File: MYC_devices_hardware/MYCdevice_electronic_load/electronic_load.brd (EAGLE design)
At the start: 136.5 x 53.6 mm, 129 parts, among them IC1 MEGA16-P, IC10 Gate7, IC11 LF347N, IC12 LF347N, IC14 MCP603CH, IC15 MCP603CH, IC16 MCP603CH, IC17 MCP603CH, IC18 MCP603CH, IC19 MCP603CH, IC2 MAX232, IC20 MCP603CH, IC3 7805TV, IC4 Gate1, IC5 Gate2, IC6 Gate3, IC7 Gate4, IC8 Gate5, IC9 Gate6, Q1 20MHz, X1 8-15V, X2 1503_09, X3 1503_09, X4 RS232

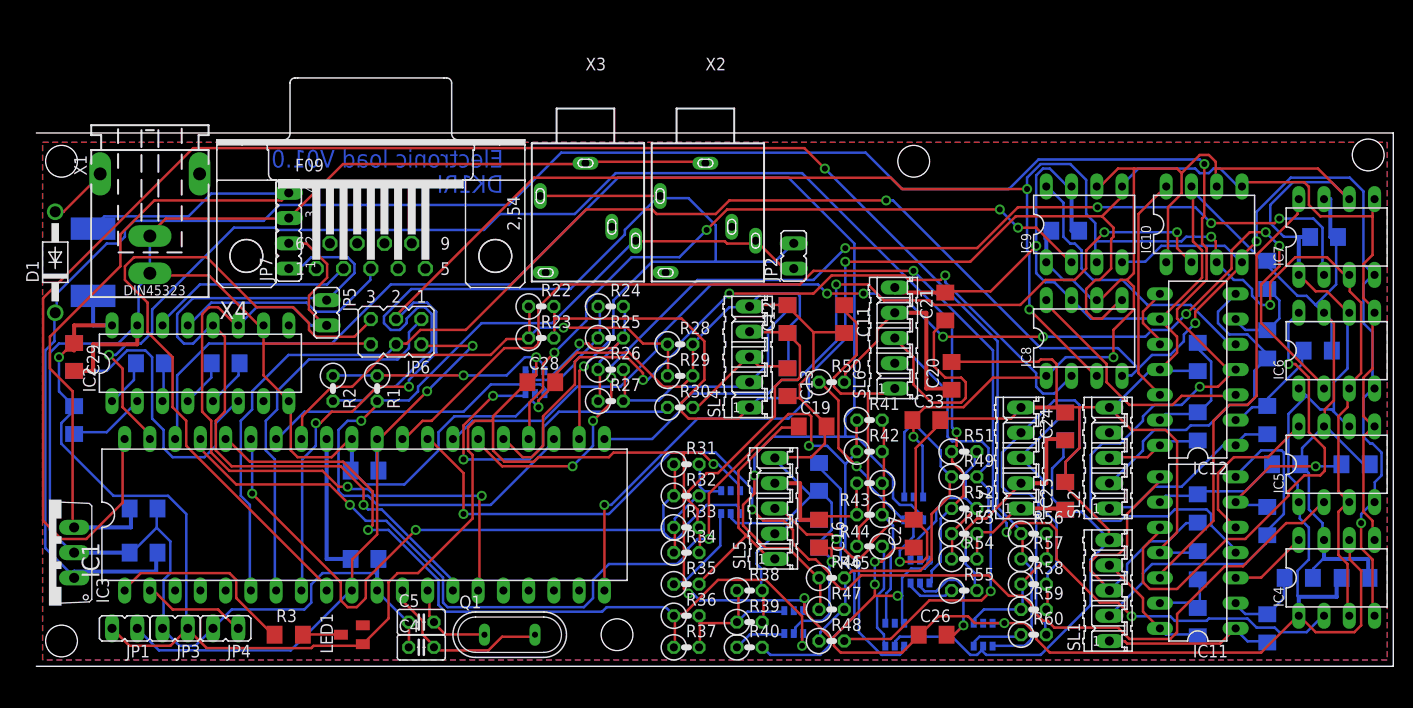
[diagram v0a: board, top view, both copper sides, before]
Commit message: deleted duplicate MYCdevice_electronic_load
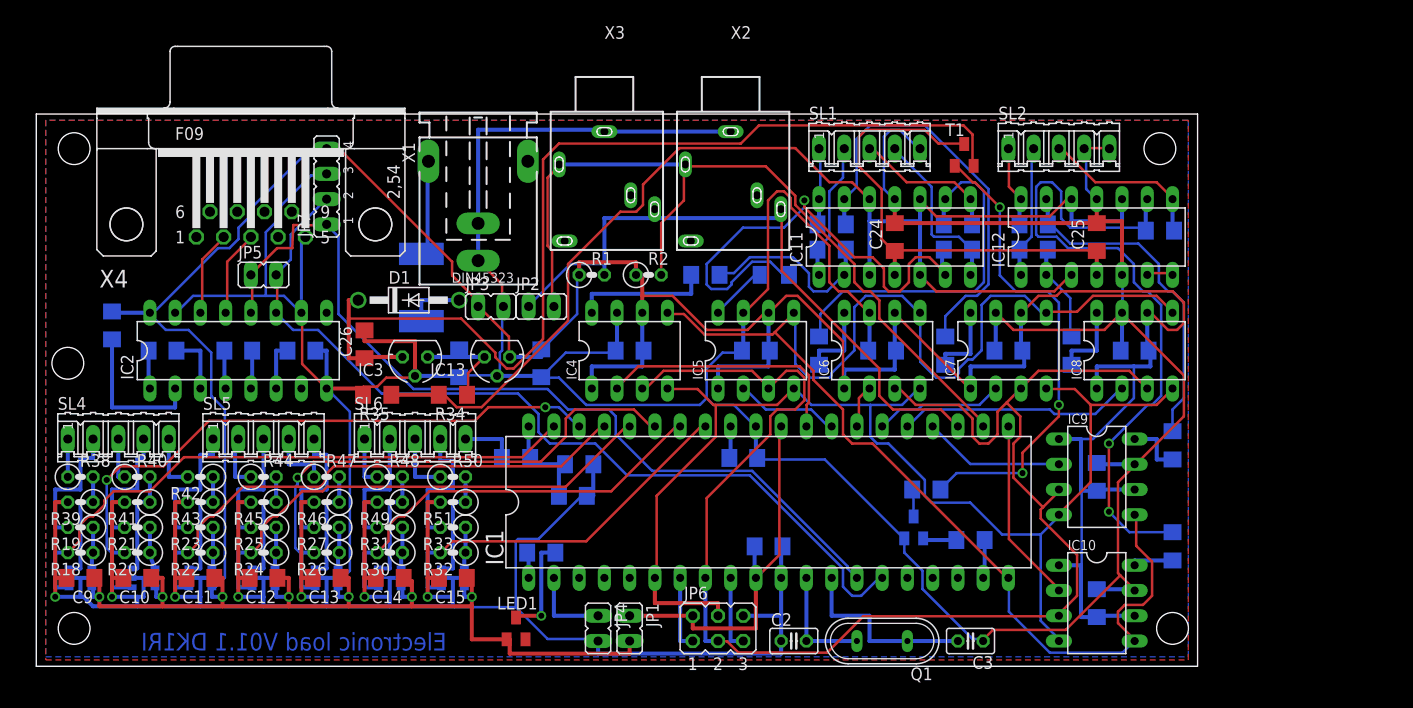
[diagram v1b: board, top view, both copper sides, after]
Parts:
- removed C29, C30, C31, C32, C33: 22uF 1210, rcl:C1206
- removed R52, R57: 27k, resistor:0207/2V
- removed R53, R58: 1k 1%, resistor:0207/2V
- removed R54: 9k53, resistor:0207/2V
- removed R55, R60: 22k, resistor:0207/2V
- removed R56: 9k1 1%, resistor:0207/2V
- removed R59: 9k52, resistor:0207/2V
- removed SL7: U/Iin, con-amp-quick:05P
- added IC13: 78L5, v-reg:78LXX
- added R18, R20: 154k, resistor:0207/2V
- added R19, R21: 18k, resistor:0207/2V
- added T1: BC807, transistor:SOT23-BEC
- added T2: BC817, transistor:SOT23-BEC
- C10, C9: value 22u 1210 -> 22uF 1210
- C11, C12, C13, C14, C15, C16, C17, C18, C19, C20, C21, C22, C23, C24, C25: value 22u -> 22uF 1210; device resistor:C1206 -> rcl:C1206
- C2, C3: value 22uF 1210 -> 18pF; device rcl:C1206 -> resistor:C025-025X050
- C28: value 22uF 1210 -> 1u; device rcl:C1206 -> resistor:C1206
- C4: value 18pF -> 22uF 1210; device resistor:C025-025X050 -> rcl:C1206
- C5: value 18pF -> 22u 1210; device resistor:C025-025X050 -> rcl:C1206
- C6: value 22uF 1210 -> 22u 1210
- IC10: value Gate7 -> MCP4921
- IC11, IC12: value LF347N -> LM324N
- IC3: value 7805TV -> 79L09; device linear:TO220V -> v-reg:78LXX
- IC4: value Gate1 -> MCP4921
- IC5: value Gate2 -> MCP4921
- IC6: value Gate3 -> MCP4921
- IC7: value Gate4 -> MCP4921
- IC8: value Gate5 -> MCP4921
- IC9: value Gate6 -> MCP4921
- L1: value (none) -> 22u
- R10, R12, R14, R16, R4, R6, R8: value 10k -> 12k
- R11, R13, R15, R17, R5, R7, R9: value 10k -> 8k2
- R22: value 68k 1% -> 154k
- R23: value na -> 18k
- R24: value 9k1 1% -> 154k
- R25: value 27k -> 18k
- R26, R38, R48: value 1k 1% -> 154k
- R27, R39, R49: value 9k53 -> 18k
- R28: value 1,8 1% -> 1k5; device resistor:0207/2V -> resistor:R1206
- R29: value 220k -> 180; device resistor:0207/2V -> resistor:R1206
- R30, R40, R50: value 22k -> 154k
- R31, R41, R46, R51: value 9k1 1% -> 18k
- R32, R42, R47: value 27k -> 154k
- R33, R43: value 1k 1% -> 18k
- R34: value 9k53 -> 8k2; device resistor:0207/2V -> resistor:R1206
- R35: value 22k -> 18k; device resistor:0207/2V -> resistor:R1206
- R36: value 9k1 1% -> 10k; device resistor:0207/2V -> resistor:R1206
- R37: value 27k -> 10k; device resistor:0207/2V -> resistor:R1206
- R44: value 9k53 -> 154k
- R45: value 22k -> 18k
- SL1: value Gates -> Gates1
- SL2: value Gates -> Gates2
- SL4, SL5: value U/Iin -> Iin
- moved IC4 74.7 mm to (59.7, 31.8)
- moved R41 74.1 mm to (10.2, 16.5), turned to 180 degrees
- moved C11 69.8 mm to (16.5, 8.89), turned to 180 degrees
- moved R39 68.4 mm to (4.45, 16.5), turned to 180 degrees
- moved R38 68.3 mm to (4.45, 19.1)
- moved R42 67.4 mm to (16.5, 19.1), turned to 180 degrees
- moved R43 67.3 mm to (16.5, 16.5)
- moved R5 67.0 mm to (67.3, 39.4), turned to 0 degrees
- moved C2 66.8 mm to (76.2, 2.54), flipped to the top, turned to 0 degrees
- moved C26 64.2 mm to (33.0, 32.4), turned to 90 degrees
- moved SL4 64.0 mm to (8.26, 22.9), turned to 0 degrees
- moved R40 63.9 mm to (10.2, 19.1)
- moved IC17 63.8 mm to (22.9, 8.89), turned to 90 degrees
- moved C3 61.5 mm to (94.0, 2.54), flipped to the top, turned to 180 degrees
- moved R7 61.4 mm to (74.3, 39.4), turned to 0 degrees
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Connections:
- net N$29 renamed FET5
- removed net N$57 (its old number): C25.1, R53.2, R54.2, SL7.1
- removed net N$75: IC15.3, R35.1
- removed net N$77: IC16.4, R36.2, R37.2, R38.1, R39.1
- removed net N$78: C17.1, R40.2, SL5.3
- removed net N$83: IC11.3, IC4.8
- removed net N$84: IC19.4, R51.2, R52.2, R53.1, R54.1
- removed net N$85: IC19.3, R55.1
- removed net N$86: C24.1, R55.2, SL7.2
- removed net N$87: IC20.4, R56.2, R57.2, R58.1, R59.1
- removed net N$88: C22.1, R60.2, SL7.4
- removed net N$92: IC11.1, R4.2, SL1.1
- removed net N$93: IC10.8, IC12.12
- removed net N$94: IC12.13, R16.1, R17.1
- removed net N$95: IC12.14, R16.2, SL2.3
- new net 9V: C27.1, IC13.IN, IC3.OUT, R34.1
- new net FET1: IC12.8, R16.2, SL2.3
- new net FET2: IC12.1, R12.2, SL2.2
- new net FET3: IC12.14, R14.2, SL2.1
- new net FET4: IC11.7, R6.2, SL1.4
- new net FET6: IC11.1, R4.2, SL1.2
- new net FET7: IC11.14, R10.2, SL1.1
- new net GON: IC1.19, R36.1
- new net N$27: R29.2, SL6.5
- new net N$29: R21.2, SL4.4
- new net N$32: IC20.4, R32.1, R33.1
- new net N$39: IC10.8, R17.2
- new net N$41: IC16.4, R22.1, R23.1
- new net N$45: IC17.4, R24.1, R25.1
- new net N$52: R48.1, SL6.1
- new net N$53: R31.2, SL6.2
- new net N$55: IC5.8, R7.2
- new net N$64: R36.2, T2.B
- new net N$65: R38.1, SL4.1
- new net N$72: IC18.3, R46.1, R47.2
- new net VREF: IC11.10, IC11.12, IC11.3, IC11.5, IC12.10, IC12.12, IC12.3, R34.2, R35.1
- net C13: now also C5.1; no longer C7.1
- net GND: now also C1.1, C10.2, C2.1, C4.2, C8.1, C9.2, IC12.5, IC13.GND, IC14.5, IC15.5, IC16.5, IC17.5, IC18.5, IC19.5, IC20.5, IC3.GND, R35.2, R39.2, R41.2, R43.2, R45.2, R46.2, R49.2, R51.2, SL2.4, T2.E, X4.5; no longer C1.2, C10.1, C2.2, C29.2, C30.2, C31.2, C32.2, C33.2, C4.1, C5.1, C6.2, IC12.9, IC3.2, R11.2, R13.2, R15.2, R17.2, R29.2, R5.2, R7.2, R9.2, SL4.5, SL5.5, SL6.5, SL7.5
- net I1: now also IC1.39, R18.2; no longer IC1.34, R24.1, R25.1
- net I2: now also IC1.38, R20.2; no longer IC1.35, R31.1, R32.1
- net I3: now also IC1.37, R22.2; no longer IC1.36, R36.1, R37.1
- net I4: now also IC1.36, R24.2; no longer IC1.37, R41.1, R42.1
- net I5: now also IC1.35, R26.2; no longer IC1.38, R46.1, R47.1
- net I6: now also IC1.34, R30.2; no longer IC1.39, R51.1, R52.1
- net I7: now also IC1.33, R32.2; no longer IC1.40, R56.1, R57.1
- net N$1: now also IC14.4, R18.1, R19.1; no longer C2.1, IC3.3, JP7.4, L1.1
- net N$10: now also R9.2; no longer IC11.10
- net N$12: now also D1.A, L1.2; no longer IC11.14, R10.2, SL1.4
- net N$13: now also C6.1; no longer C8.1
- net N$14: now also C5.2; no longer C7.2
- net N$16: now also C7.1; no longer C9.1
- net N$17: now also C8.2; no longer C10.2
- net N$19: now also C2.2; no longer C4.2
- net N$21: now also R11.2; no longer IC11.12
- net N$24: now also R13.2; no longer IC12.3
- net N$25: now also C4.1; no longer C6.1
- net N$26: now also R15.2; no longer IC12.5
- net N$3: now also C6.2; no longer C8.2
- net N$30: now also IC15.4, R20.1, R21.1; no longer IC12.1, R12.2, SL2.1
- net N$31: now also IC4.8, R5.2; no longer IC12.7, R14.2, SL2.2
- net N$34: now also IC19.4, R30.1, R31.1; no longer C11.1, R45.2, SL6.1
- net N$35: now also C1.2; no longer C3.2
- net N$37: now also C3.2; no longer C5.2
- net N$40: now also IC12.13; no longer IC12.6
- net N$44: now also IC17.3, R45.1; no longer C16.1, R43.2, SL5.4
- net N$47: now also IC18.4, R26.1, R27.1; no longer C19.1, R35.2, SL5.1
- net N$48: now also R47.1, SL5.4; no longer IC17.4, R41.2, R42.2, R43.1, R44.1
- net N$49: now also IC15.3, R40.2, R41.1; no longer C12.1, R33.2, R34.2, SL4.4
- net N$54: now also R25.2, SL5.3; no longer IC17.3, R45.1
- net N$56: now also C26.1, IC3.IN, T1.E; no longer C1.1, IC11.4, IC12.4, IC3.1
- net N$58: now also IC12.9, R16.1, R17.1; no longer IC18.4, R46.2, R47.2, R48.1, R49.1
- net N$59: now also C24.1, C25.1, IC11.4, IC12.4, T1.C; no longer C20.1, R50.2, SL6.4
- net N$60: now also R27.2, SL5.5; no longer IC18.3, R50.1
- net N$61: now also R37.2, T1.B; no longer C21.1, R48.2, R49.2, SL6.3
- net N$63: now also R37.1, T2.C; no longer IC11.5, IC5.8
- net N$66: now also R40.1, SL4.3; no longer C15.1, R22.2, R23.2, SL4.1
- net N$67: now also IC14.3, R38.2, R39.1; no longer IC14.4, R24.2, R25.2, R26.1, R27.1
- net N$68: now also R42.2, SL4.5; no longer C13.1, R30.2, SL4.3
- net N$69: now also R19.2, SL4.2; no longer IC14.3, R30.1
- net N$7: now also L1.1; no longer D1.A
- net N$70: now also R44.1, SL5.2; no longer C14.1, R26.2, R27.2, SL4.2
- net N$74: now also IC19.3, R48.2, R49.1; no longer IC15.4, R31.2, R32.2, R33.1, R34.1
- net N$76: now also R50.1, SL6.3; no longer IC11.7, R6.2, SL1.2
- net N$79: now also R23.2, SL5.1; no longer IC16.3, R40.1
- net N$80: now also IC16.3, R42.1, R43.1; no longer C18.1, R38.2, R39.2, SL5.2
- net N$89: now also R33.2, SL6.4; no longer IC20.3, R60.1
- net N$90: now also IC20.3, R50.2, R51.1; no longer C23.1, R58.2, R59.2, SL7.3
- net N$96: now also IC12.6, IC12.7; no longer IC12.10, IC12.8
- net U: now also C28.1, IC1.40; no longer IC1.33, R22.1, R23.1
- net VDD: now also C10.1, C11.1, C12.1, C13.1, C14.1, C15.1, C16.1, C17.1, C18.1, C19.1, C20.1, C21.1, C22.1, C23.1, C7.2, C9.1, IC13.OUT, JP7.4; no longer C26.1, C27.1, C28.1, C29.1, C30.1, C31.1, C32.1, C33.1, C9.2, L1.2
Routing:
- net I7: track 185.5 -> 38.1 mm, vias 1 -> 0
- net N$56: track 233.5 -> 101.7 mm, vias 2 -> 0
- net VREF: track 0.00 -> 129.2 mm
- net N$71: track 116.2 -> 4.42 mm, vias 7 -> 0
- net N$62: track 116.5 -> 10.5 mm, vias 2 -> 0
- net N$50: track 130.2 -> 25.9 mm, vias 3 -> 0
- net N$20: track 222.5 -> 124.3 mm, vias 4 -> 0
- net I6: track 138.8 -> 42.9 mm, vias 2 -> 0
- net I5: track 149.1 -> 54.7 mm
- net N$51: track 106.8 -> 13.0 mm, vias 7 -> 0
- net VDD: track 480.1 -> 391.5 mm, vias 12 -> 7
- net N$1: track 81.1 -> 4.25 mm
- net N$28: track 222.6 -> 150.5 mm, vias 6 -> 0
- net I4: track 118.8 -> 50.5 mm, vias 3 -> 0
- net N$18: track 70.7 -> 7.62 mm
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- added copper zone on layer 16, net VDD
- removed copper zone on layer 16, net GND
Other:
- board size 136.5 x 53.6 mm -> 116.8 x 55.5 mm
- board text added: "Electronic load V01.1 DK1RI"
- board text removed: "DK1RI"
- board text removed: "Electronic load V01.0"

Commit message: new Hardware for electronic load, firmware and description adapted
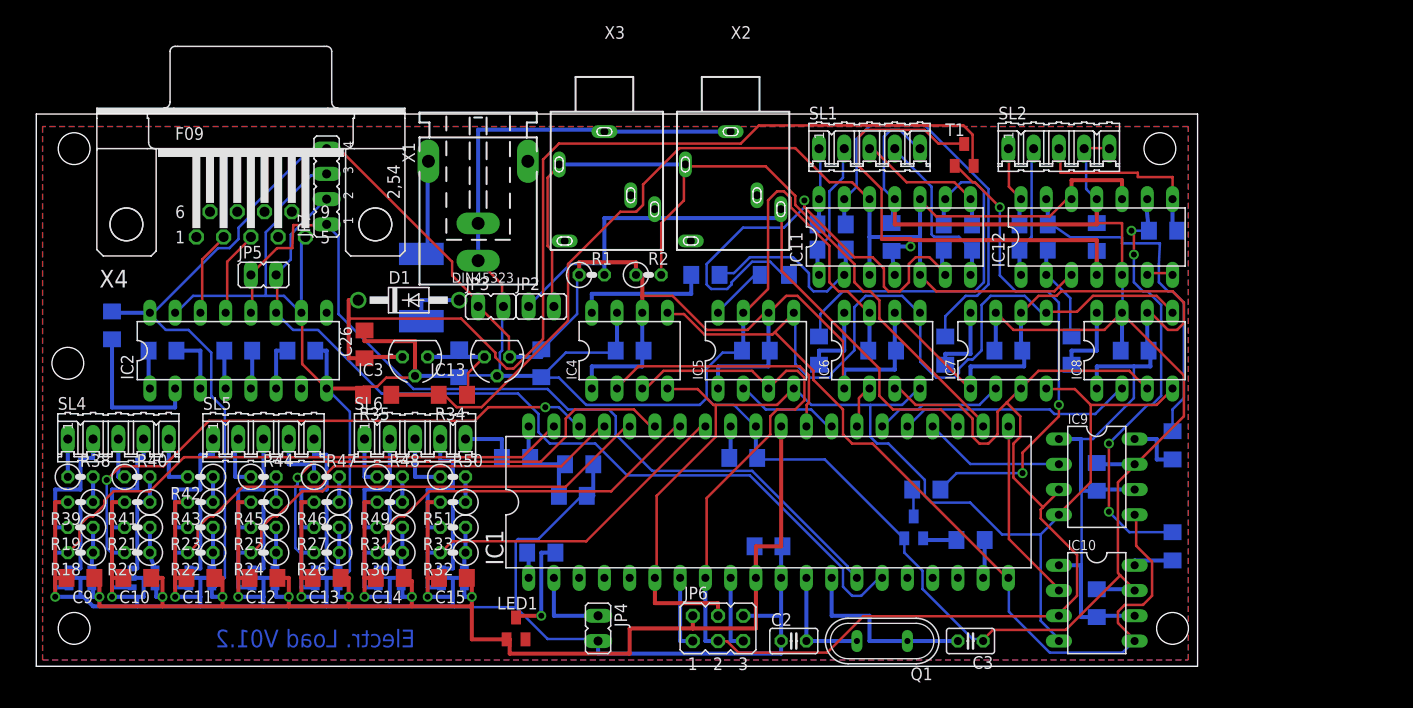
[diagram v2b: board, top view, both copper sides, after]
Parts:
- removed JP1: Power, jumper:JP1
- IC14, IC15, IC16, IC17, IC18, IC19, IC20: value MCP603CH -> MCP6031
- R34: value 8k2 -> 1k3
- R35: value 18k -> 1k
- R38, R40, R42, R44, R47, R48, R50: value 154k -> 18k
- R39, R43, R45, R46, R49, R51: value 18k -> 154k
- R41: value 18k -> 154
- moved C24 0.32 mm to (86.0, 43.2), flipped to the bottom
- moved R16 0.32 mm to (113.3, 43.8)
- flipped C25 to the bottom
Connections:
- net N$11 renamed LDAC
- net N$23 renamed S6
- net N$4 renamed S7
- net N$50 renamed S2
- net N$51 renamed S1
- net N$62 renamed S4
- net N$71 renamed S3
- net N$8 renamed S5
- removed net N$25: C4.1, IC1.10, IC1.30, JP1.1, JP6.2
- net FET1: now also IC11.14, R10.2, SL1.1; no longer IC12.8, R16.2, SL2.3
- net FET2: now also IC11.1, R4.2, SL1.2; no longer IC12.1, R12.2, SL2.2
- net FET3: now also IC11.8, R8.2, SL1.3; no longer IC12.14, R14.2, SL2.1
- net FET5: now also IC12.14, R14.2, SL2.1; no longer IC11.8, R8.2, SL1.3
- net FET6: now also IC12.1, R12.2, SL2.2; no longer IC11.1, R4.2, SL1.2
- net FET7: now also IC12.8, R16.2, SL2.3; no longer IC11.14, R10.2, SL1.1
- net VDD: now also C4.1, IC1.10, IC1.30, JP6.2; no longer JP1.2
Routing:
- net VDD: track 391.5 -> 432.9 mm
- net N$25: track 38.7 -> 0.00 mm
- net N$58: track 70.1 -> 45.1 mm, vias 2 -> 4
- net FET7: track 7.87 -> 20.1 mm
- net FET1: track 17.0 -> 7.87 mm
- net N$59: track 49.7 -> 56.8 mm, vias 0 -> 1
- net FET5: track 14.9 -> 8.19 mm
- net FET3: track 8.19 -> 14.9 mm
- net GND: track 661.4 -> 666.9 mm
- net N$40: track 34.1 -> 35.7 mm
- net VREF: track 129.2 -> 128.6 mm
- net FET6: track 13.9 -> 13.3 mm
- net FET2: track 13.3 -> 13.9 mm
- added copper zone on layer 16, net GND
- removed copper zone on layer 16, net VDD
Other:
- board text added: "Electr. Load V01.2"
- board text removed: "Electronic load V01.1 DK1RI"

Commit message: board: 3V I2c, bascom: include files used
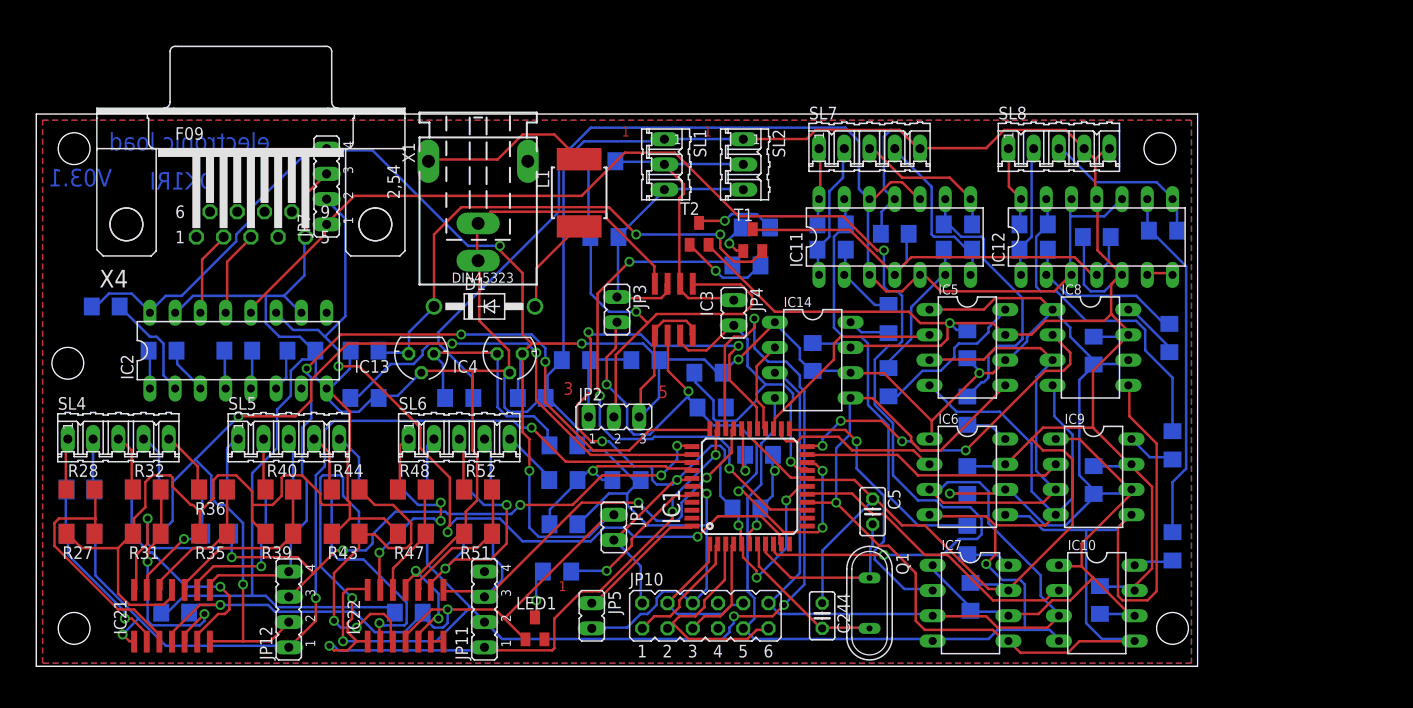
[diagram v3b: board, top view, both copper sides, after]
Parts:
- removed C23, C24, C25, C26, C27: 22uF 1210, rcl:C1206
- removed C28: 1u, resistor:C1206
- removed IC15, IC16, IC17, IC18, IC19, IC20: MCP6031, linear:SOT23-6
- removed JP6: ISP, jumper:JP3Q
- removed R12: 12k, resistor:R1206
- removed X2, X3: 1503_09, con-lumberg:1503_09
- added C244: 18pF, resistor:C025-025X050
- added IC21, IC22: MCP60x4, linear:SO14
- added JP1: Power, jumper:JP1
- added JP10: (no value), jumper:JP6Q
- added JP11, JP12: (no value), jumper:JP4
- added R52: 18k, resistor:M1206
- added R53: 180, resistor:R1206
- added R54: 1k5, resistor:R1206
- added R666: 12k, resistor:R1206
- added R999: 8k2, resistor:R1206
- added SL7: Gates1, con-amp-quick:05P
- added SL8: Gates2, con-amp-quick:05P
- C1, C10, C11, C12, C13, C14, C15, C16, C17, C18, C19, C20, C21, C4, C9: value 22uF 1210 -> 22uF
- C2, C3: value 18pF -> 22uF; device resistor:C025-025X050 -> rcl:C1206
- C22: value 22uF 1210 -> 1u; device rcl:C1206 -> resistor:C1206
- C5: value 22u 1210 -> 18pF; device rcl:C1206 -> resistor:C025-025X050
- C6, C7, C8: value 22u 1210 -> 22uF
- IC1: value MEGA16-P -> ATMEGA644A; device atmel:DIL40 -> atmel:TQFP44
- IC13: value 78L5 -> 79L09
- IC14: value MCP6031 -> MCP4921; device linear:SOT23-6 -> dac:DIL08
- IC3: value 79L09 -> PCA9517; device v-reg:78LXX -> PCA9517:SO-08
- IC4: value MCP4921 -> 78L5; device dac:DIL08 -> v-reg:78LXX
- JP2: value I2C -> 3V/5V; device jumper:JP1 -> jumper:JP2
- JP3: value 5V -> SDA
- JP4: value Reset -> SCL
- JP5: value Rs232-TTL -> Reset
- R1, R2: value 4k7 -> see manual; device resistor:0207/2V -> resistor:R1206
- R10: value 12k -> 10k
- R11: value 8k2 -> 4k7
- R18, R20, R22, R24: value 154k -> 12k; device resistor:0207/2V -> resistor:R1206
- R19, R21, R23: value 18k -> 8k2; device resistor:0207/2V -> resistor:R1206
- R25, R27, R33, R47: value 18k -> 154k; device resistor:0207/2V -> resistor:M1206
- R26, R30, R32, R46: value 154k -> 18k; device resistor:0207/2V -> resistor:M1206
- R28: value 1k5 -> 18k
- R29: value 180 -> 154k; device resistor:R1206 -> resistor:M1206
- R3: value 4k7 -> see manual
- R31: value 18k -> 154; device resistor:0207/2V -> resistor:M1206
- R34: value 1k3 -> 18k; device resistor:R1206 -> resistor:M1206
- R35: value 1k -> 154k; device resistor:R1206 -> resistor:M1206
- R36: value 10k -> 18k; device resistor:R1206 -> resistor:M1206
- R37: value 10k -> 154k; device resistor:R1206 -> resistor:M1206
- R38, R39, R40, R42, R43, R44, R45, R48, R49, R50, R51: device resistor:0207/2V -> resistor:M1206
- R4: value 12k -> see manual
- R41: value 154 -> 154k; device resistor:0207/2V -> resistor:M1206
- R5: value 8k2 -> 1k
- R6: value 12k -> 1k5
- R7: value 8k2 -> 1k3
- R8: value 12k -> 1k
- R9: value 8k2 -> 10k
- SL1: value Gates1 -> I2c; device con-amp-quick:05P -> con-amp-quick:03P
- SL2: value Gates2 -> I2C; device con-amp-quick:05P -> con-amp-quick:03P
- moved R19 111.2 mm to (114.0, 33.0), flipped to the bottom, turned to 270 degrees
- moved R21 104.5 mm to (114.3, 22.2), flipped to the bottom, turned to 270 degrees
- moved R23 97.8 mm to (114.3, 12.1), flipped to the bottom, turned to 270 degrees
- moved R24 96.1 mm to (113.3, 43.8), flipped to the bottom
- moved R20 95.2 mm to (100.3, 41.9), flipped to the bottom, turned to 0 degrees
- moved R22 90.1 mm to (100.3, 44.5), flipped to the bottom, turned to 0 degrees
- moved C12 84.2 mm to (107.0, 6.67), flipped to the bottom, turned to 90 degrees
- moved R18 82.5 mm to (80.0, 44.5), flipped to the bottom, turned to 0 degrees
- moved IC14 76.8 mm to (78.1, 30.8), flipped to the top, turned to 270 degrees
- moved R36 76.4 mm to (17.8, 17.8), flipped to the top, turned to 180 degrees
- moved C5 73.2 mm to (84.1, 15.6), flipped to the top, turned to 270 degrees
- moved C13 68.6 mm to (93.7, 32.4), flipped to the bottom, turned to 90 degrees
- moved R37 65.2 mm to (24.4, 13.3)
- moved R8 62.2 mm to (33.0, 27.0)
- moved C14 58.9 mm to (93.7, 18.7), flipped to the bottom, turned to 90 degrees
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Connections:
- removed net S1: IC1.26, IC7.2
- removed net S2: IC1.29, IC4.2
- removed net S3: IC1.27, IC6.2
- removed net S4: IC1.28, IC5.2
- removed net S5: IC1.24, IC9.2
- removed net S6: IC1.25, IC8.2
- removed net S7: IC1.21, IC10.2
- new net N$11: C5.2, IC1.8, Q1.1
- new net N$23: IC1.1, JP10.10, JP10.4
- new net N$25: C3.2, IC1.29
- new net N$4: C4.1, IC1.17, IC1.27, IC1.38, IC1.5, JP1.2, JP10.2
- new net N$50: IC1.19, IC3.7, JP4.2, R4.2
- new net N$51: JP2.1, R5.1, R6.2
- new net N$62: IC3.1, JP2.2, R1.1, R2.1
- new net N$8: IC22.6, IC22.7
- new net SFET1: IC11.14, R18.2, SL7.1
- new net SFET2: IC11.1, R14.2, SL7.2
- new net SFET3: IC11.8, R16.2, SL7.3
- new net SFET4: IC11.7, R666.2, SL7.4
- new net SFET5: IC12.14, R22.2, SL8.1
- new net SFET6: IC12.1, R20.2, SL8.2
- new net SFET7: IC12.8, R24.2, SL8.3
- net 9V: now also C20.1, IC13.OUT, IC4.IN, R7.1; no longer C27.1, IC13.IN, IC3.OUT, R34.1
- net C13: now also C6.1; no longer C5.1
- net FET1: now also IC1.23, IC7.2; no longer IC11.14, R10.2, SL1.1
- net FET2: now also IC1.26, IC14.2; no longer IC11.1, R4.2, SL1.2
- net FET3: now also IC1.24, IC6.2; no longer IC11.8, R8.2, SL1.3
- net FET4: now also IC1.25, IC5.2; no longer IC11.7, R6.2, SL1.4
- net FET5: now also IC1.21, IC9.2; no longer IC12.14, R14.2, SL2.1
- net FET6: now also IC1.22, IC8.2; no longer IC12.1, R12.2, SL2.2
- net FET7: now also IC1.16, IC10.2; no longer IC12.8, R16.2, SL2.3
- net GND: now also C1.2, C2.2, C244.1, C5.1, C9.1, IC1.18, IC1.28, IC1.39, IC1.6, IC14.7, IC21.11, IC22.11, IC22.5, IC3.4, IC4.GND, JP10.6, JP5.2, R27.2, R31.2, R47.2, R54.2, R6.1, R8.2, SL1.1, SL2.1, SL7.5, SL8.4, SL8.5; no longer C1.1, C2.1, C23.2, C24.2, C25.2, C26.2, C27.2, C28.2, C8.1, C9.2, IC1.11, IC1.31, IC14.2, IC14.5, IC15.2, IC15.5, IC16.2, IC16.5, IC17.2, IC17.5, IC18.2, IC18.5, IC19.2, IC19.5, IC20.2, IC20.5, IC3.GND, IC4.7, JP3.2, JP4.2, JP6.6, R28.2, R41.2, R45.2, R46.2, R49.2, SL1.5, SL2.4, SL2.5, X2.1, X3.1
- net GON: now also IC1.14, R10.1; no longer IC1.19, R36.1
- net I1: now also IC1.36, IC21.1, JP12.1, R25.2; no longer IC1.39, IC14.1, R18.2
- net I2: now also IC1.35, IC21.7, JP12.2, R29.2; no longer IC1.38, IC15.1, R20.2
- net I3: now also IC1.34, IC21.14, JP12.3, R33.2; no longer IC1.37, IC16.1, R22.2
- net I4: now also IC1.33, IC21.8, JP12.4, R37.2; no longer IC1.36, IC17.1, R24.2
- net I5: now also IC1.32, IC22.1, JP11.1, R41.2; no longer IC1.35, IC18.1, R26.2
- net I6: now also IC1.31, IC22.14, JP11.2, R45.2; no longer IC1.34, IC19.1, R30.2
- net I7: now also IC1.30, IC22.8, JP11.3, R49.2; no longer IC1.33, IC20.1, R32.2
- net LDAC: now also IC1.15, IC14.5; no longer IC1.20, IC4.5
- net N$1: now also IC21.2, R25.1, R26.1; no longer IC14.4, R18.1, R19.1
- net N$10: now also R999.2; no longer R9.2
- net N$13: now also C7.1; no longer C6.1
- net N$14: now also C6.2; no longer C5.2
- net N$15: now also IC1.2, JP10.1; no longer IC1.7, JP6.1
- net N$16: now also C8.1; no longer C7.1
- net N$17: now also C9.2; no longer C8.2
- net N$18: now also IC1.4, JP10.5; no longer IC1.9, JP6.5
- net N$19: now also C244.2, IC1.7; no longer C2.2, IC1.12
- net N$2: now also IC1.9; no longer IC1.14, JP5.1
- net N$20: now also IC14.4, JP10.9; no longer IC1.6, IC4.4, JP6.4
- net N$21: now also R17.2; no longer R11.2
- net N$22: now also IC3.2, JP4.1, SL1.2, SL2.2; no longer IC1.22, JP2.2, X2.2, X3.2
- net N$24: now also R19.2; no longer R13.2
- net N$26: now also R21.2; no longer R15.2
- net N$27: now also R53.2; no longer R29.2
- net N$28: now also IC14.3, JP10.12; no longer IC1.8, IC4.3, JP6.3
- net N$29: now also R30.2; no longer R21.2
- net N$3: now also C7.2; no longer C6.2
- net N$30: now also IC21.6, R29.1, R30.1; no longer IC15.4, R20.1, R21.1
- net N$31: now also IC14.8, R13.2; no longer IC4.8, R5.2
- net N$32: now also IC22.9, R49.1, R50.1; no longer IC20.4, R32.1, R33.1
- net N$34: now also IC22.13, R45.1, R46.1; no longer IC19.4, R30.1, R31.1
- net N$35: now also IC1.20, IC3.6, JP3.2, R3.2; no longer C1.2, IC1.32
- net N$36: now also R17.1, R18.1; no longer R10.1, R11.1
- net N$37: now also IC1.44, JP5.1; no longer C3.2, IC1.13, Q1.1
- net N$38: now also R16.1, R999.1; no longer R8.1, R9.1
- net N$39: now also R23.2; no longer R17.2
- net N$40: now also R21.1, R22.1; no longer R14.1, R15.1
- net N$41: now also IC21.13, R33.1, R34.1; no longer IC16.4, R22.1, R23.1
- net N$42: now also IC1.40, R11.1; no longer IC1.1, R3.1
- net N$43: now also R11.2; no longer R3.2
- net N$44: now also IC21.10, R39.1, R40.2; no longer IC17.3, R44.2, R45.1
- net N$45: now also IC21.9, R37.1, R38.1; no longer IC17.4, R24.1, R25.1
- net N$46: now also IC1.3, JP10.11, JP10.3; no longer IC1.2, JP4.1
- net N$47: now also IC22.2, R41.1, R42.1; no longer IC18.4, R26.1, R27.1
- net N$48: now also R44.1; no longer R47.1
- net N$49: now also IC21.5, R31.1, R32.2; no longer IC15.3, R40.2, R41.1
- net N$5: now also IC3.3, JP3.1, SL1.3, SL2.3; no longer IC1.23, JP2.1, X2.3, X3.3
- net N$53: now also R46.2; no longer R31.2
- net N$54: now also R38.2; no longer R25.2
- net N$55: now also R15.2; no longer R7.2
- net N$56: now also C19.1, IC13.IN; no longer C26.1, IC3.IN
- net N$57: now also R19.1, R20.1; no longer R12.1, R13.1
- net N$58: now also R23.1, R24.1; no longer R16.1, R17.1
- net N$59: now also C1.1, C21.1; no longer C24.1, C25.1
- net N$6: now also IC1.10; no longer IC1.15, JP5.2
- net N$60: now also R42.2; no longer R27.2
- net N$61: now also R9.2; no longer R37.2
- net N$63: now also R9.1; no longer R37.1
- net N$64: now also R10.2; no longer R36.2
- net N$65: now also R28.1; no longer R38.1
- net N$66: now also R32.1; no longer R40.1
- net N$67: now also IC21.3, R27.1, R28.2; no longer IC14.3, R38.2, R39.1
- net N$68: now also R36.2; no longer R42.2
- net N$69: now also R26.2; no longer R19.2
- net N$70: now also R40.1; no longer R44.1
- net N$72: now also IC22.3, R43.1, R44.2; no longer IC18.3, R46.1, R47.2
- net N$73: now also R15.1, R666.1; no longer R6.1, R7.1
- net N$74: now also IC22.12, R47.1; no longer IC19.3, R49.1
- net N$76: now also R52.1; no longer R50.1
- net N$79: now also R34.2; no longer R23.2
- net N$80: now also IC21.12, R35.1, R36.1; no longer IC16.3, R42.1, R43.1
- net N$89: now also R50.2; no longer R33.2
- net N$90: now also IC22.10, R52.2; no longer IC20.3, R50.2
- net N$91: now also R13.1, R14.1; no longer R4.1, R5.1
- net U: now also C22.1, IC1.37, R53.1, R54.1; no longer C28.1, IC1.40, R28.1, R29.1
- net VDD: now also C2.1, C8.2, IC14.1, IC21.4, IC22.4, IC3.5, IC3.8, IC4.OUT, JP1.1, JP2.3, R3.1, R4.1, R5.2; no longer C19.1, C20.1, C21.1, C22.1, C23.1, C4.1, C7.2, C9.1, IC1.10, IC1.30, IC13.OUT, IC15.6, IC16.6, IC17.6, IC18.6, IC19.6, IC20.6, IC4.1, IC4.6, JP3.1, JP6.2, R1.1, R2.1
- net VREF: now also R7.2, R8.1; no longer R34.2, R35.1
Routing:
- net N$4: track 0.00 -> 99.7 mm, vias 0 -> 7
- net I6: track 42.9 -> 111.8 mm, vias 0 -> 4
- net N$35: track 3.30 -> 59.5 mm, vias 0 -> 5
- net VDD: track 432.9 -> 378.0 mm, vias 7 -> 8
- net N$22: track 83.7 -> 32.5 mm
- net GON: track 3.96 -> 54.2 mm, vias 0 -> 3
- net N$62: track 0.00 -> 50.1 mm, vias 0 -> 1
- net N$56: track 101.7 -> 53.9 mm, vias 0 -> 2
- net N$2: track 88.8 -> 136.6 mm, vias 0 -> 2
- net N$61: track 47.8 -> 3.91 mm, vias 3 -> 1
- net N$5: track 67.4 -> 27.0 mm
- net N$50: track 0.00 -> 39.6 mm, vias 0 -> 1
- net N$73: track 50.9 -> 14.6 mm, vias 1 -> 0
- net I2: track 65.7 -> 101.8 mm, vias 2 -> 4
- net I4: track 50.5 -> 82.1 mm, vias 0 -> 3
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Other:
- board text added: "1"
- board text added: "3"
- board text added: "5"
- board text added: "DK1RI"
- board text added: "V03.1"
- board text added: "electronic load"
- board text removed: "Electr. Load V01.2"
